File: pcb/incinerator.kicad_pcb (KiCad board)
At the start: 2 copper layers, 73.7 x 76.8 mm, 51 parts, among them J1 Power Source 12V, J2 IGNITION_MAIN, J3 IGNITION_AFT, J4 VALVE_MAIN, J5 VALVE_AFT_HI, J6 VALVE_AFT_LO, J7 AIRPMP, J8 To Encoder, J9 To Display, Q1 IRLU120N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

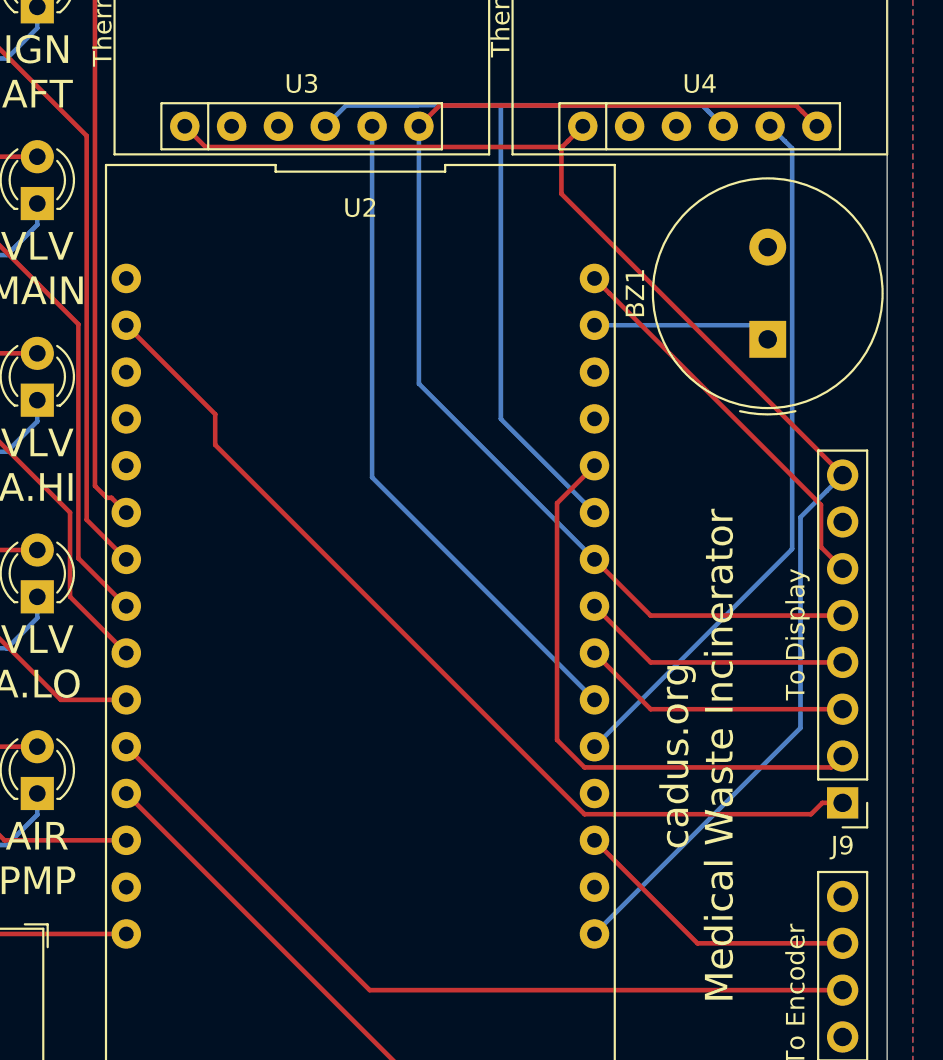
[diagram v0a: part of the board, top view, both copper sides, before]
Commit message: Increased drill sizes for breakout boards, so they can be mounted directly
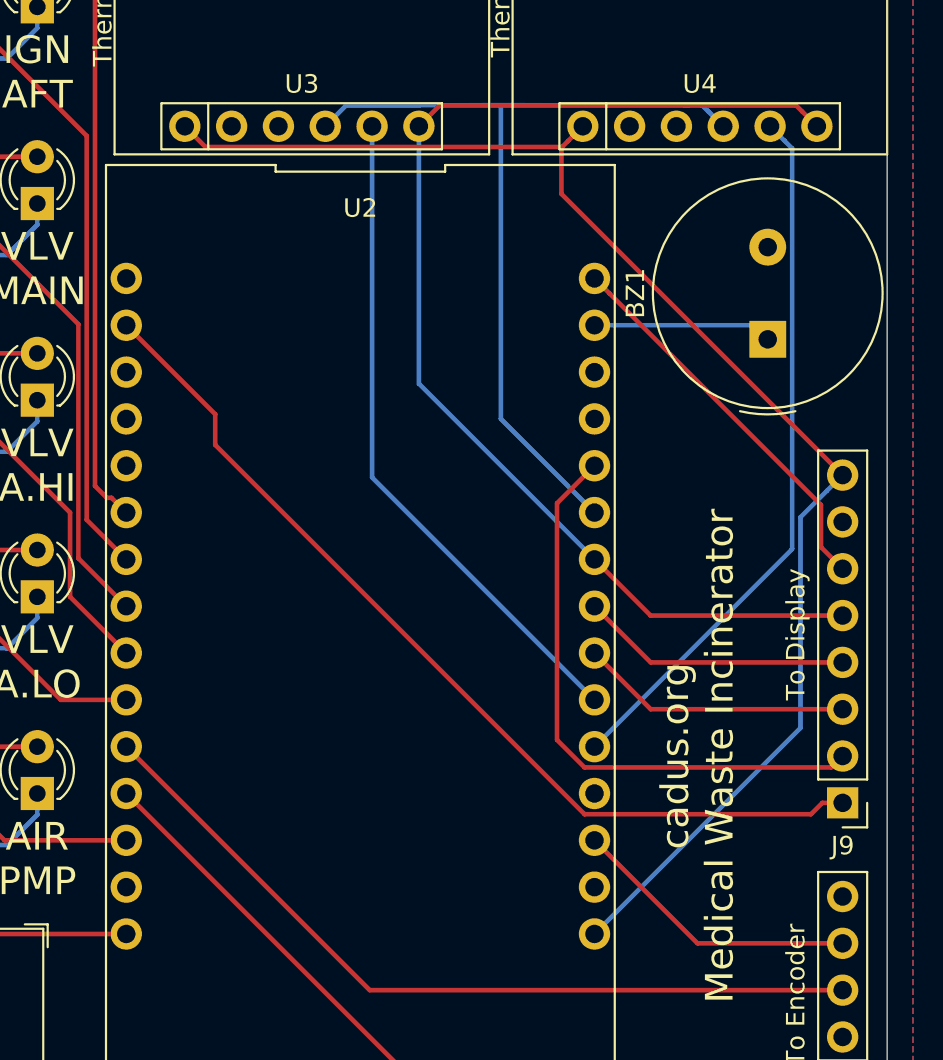
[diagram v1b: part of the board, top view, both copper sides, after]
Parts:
- U3, U4: value Adafruit_MAX31855 -> Adafruit MAX31855

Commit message: Added Open Source Hardware logo
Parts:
- added G***: LOGO, incinerator:osh, F.Cu at (146.7, 108.0)

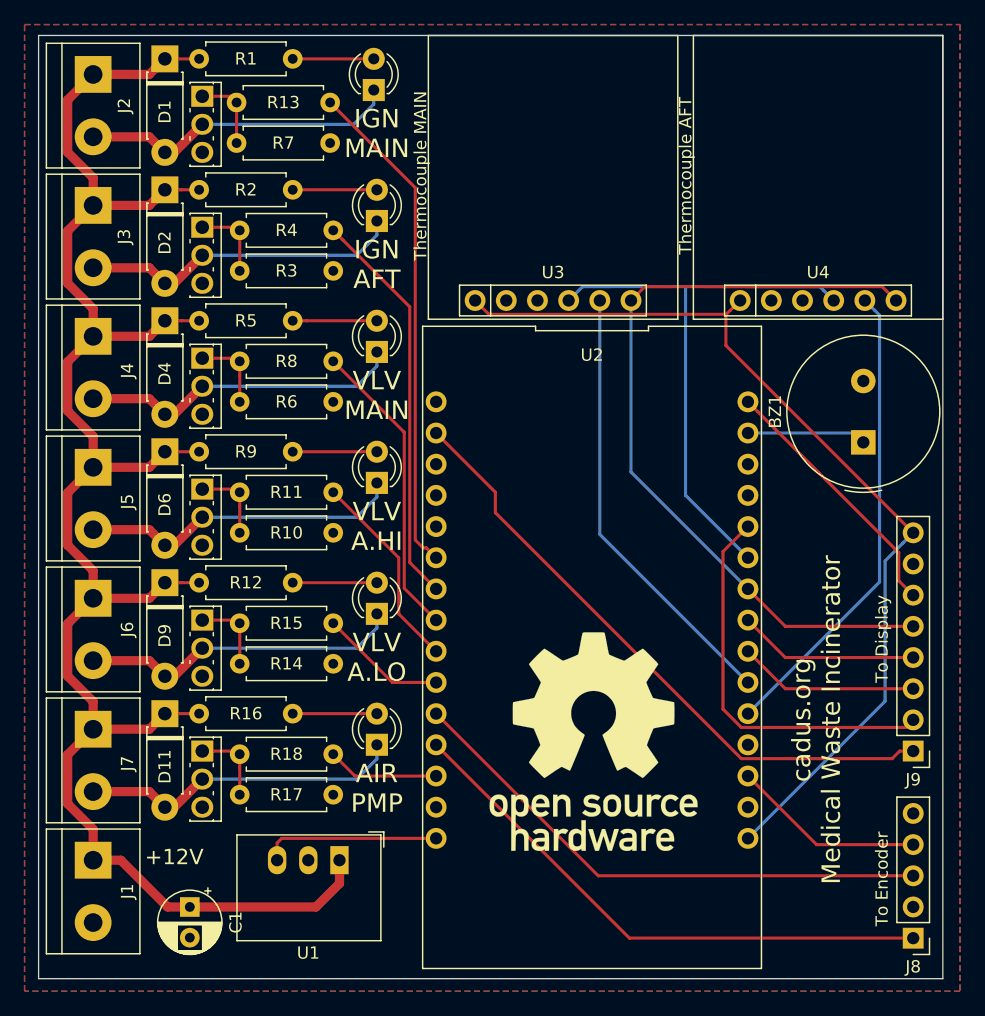
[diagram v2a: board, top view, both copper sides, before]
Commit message: pcb: Delete AFT.LO channel
Rearrange screw connectors
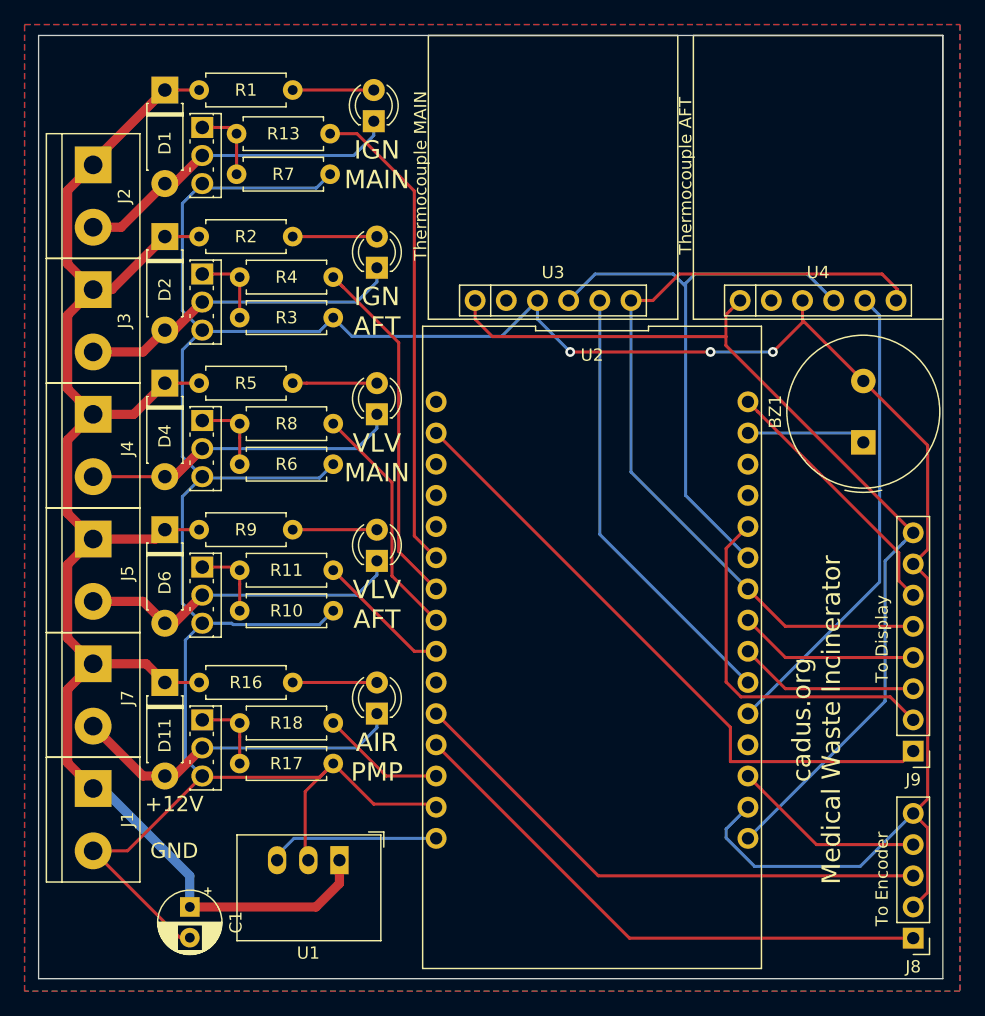
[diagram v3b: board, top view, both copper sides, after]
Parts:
- removed D10: RED, incinerator:LED_D3.0mm_Custom
- removed D9: D, incinerator:D_DO-41_P7.62mm_Custom
- removed G***: LOGO, incinerator:osh
- removed J6: VALVE_AFT_LO, TerminalBlock:TerminalBlock_bornier-2_P5.08mm
- removed Q5: IRLU120N, incinerator:SIPAK_Vertical_Custom
- removed R12: 1k, incinerator:R_THT_D2.5mm_P7.62mm_Custom
- removed R14: 15k, incinerator:R_THT_D2.5mm_P7.62mm_Custom
- removed R15: 100, incinerator:R_THT_D2.5mm_P7.62mm_Custom
- J5: value VALVE_AFT_HI -> VALVE_AFT
- U3, U4: value Adafruit MAX31855 -> Adafruit_MAX31855
- moved J2 7.37 mm to (105.9, 61.0)
- moved J3 6.86 mm to (105.9, 71.1)
- moved D8 6.35 mm to (129.0, 93.2)
- moved R11 6.35 mm to (117.9, 94.0)
- moved D6 6.35 mm to (111.8, 90.7)
- moved J4 6.35 mm to (105.9, 81.3)
- moved Q4 6.35 mm to (114.8, 93.7)
- moved R10 6.35 mm to (125.5, 97.3)
- moved R9 6.35 mm to (122.2, 90.7)
- moved J1 5.84 mm to (105.9, 111.8)
- moved J5 5.84 mm to (105.9, 91.4)
- moved J7 5.33 mm to (105.9, 101.6)
- moved D4 5.08 mm to (111.8, 78.7)
- moved D5 5.08 mm to (129.0, 81.3)
- moved Q3 5.08 mm to (114.8, 81.8)
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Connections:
- U2 pad 1: Net-(U2-Pad1) -> (no net)
- U2 pad 10: Net-(R15-Pad2) -> (no net)
- U2 pad 19: Net-(U2-Pad19) -> (no net)
- U2 pad 27: Net-(U2-Pad27) -> (no net)
- U2 pad 28: Net-(U2-Pad28) -> (no net)
- U2 pad 3: Net-(U2-Pad3) -> (no net)
- U2 pad 4: Net-(U2-Pad4) -> (no net)
- U2 pad 5: Net-(U2-Pad5) -> (no net)
- U3 pad 2: Net-(U3-Pad2) -> (no net)
- U4 pad 2: Net-(U4-Pad2) -> (no net)
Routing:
- net Earth: track 0.00 -> 271.4 mm, vias 0 -> 3
- net Net-(D10-Pad1): track 26.4 -> 0.00 mm
- net +12V: track 153.6 -> 137.3 mm
- net Net-(R15-Pad2): track 10.4 -> 0.00 mm
- net Net-(D10-Pad2): track 6.86 -> 0.00 mm
- net Net-(Q5-Pad1): track 6.46 -> 0.00 mm
- net Net-(R11-Pad2): track 16.4 -> 11.1 mm
- net Net-(R8-Pad2): track 24.6 -> 19.5 mm
- net Net-(R4-Pad2): track 32.7 -> 30.0 mm
- net /RST: track 32.1 -> 29.9 mm
- net Net-(U2-Pad25): track 47.5 -> 49.3 mm
- net +3V3: track 77.1 -> 78.8 mm
- net /CLK: track 64.9 -> 66.4 mm
- net Net-(R13-Pad2): track 40.8 -> 39.4 mm
- net Net-(D11-Pad2): track 26.4 -> 27.6 mm
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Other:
- board text added: "GND"
- board text added: "VLV AFT"
- board text removed: "VLV A.HI"
- board text removed: "VLV A.LO"
